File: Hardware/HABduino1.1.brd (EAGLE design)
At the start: 68.5 x 53.4 mm, 43 parts, among them IC2 TPS61201, U1 ARDUINO_SHIELDNO_SILK, U2 LM3480IM3-3.3, U3 TXS0102DCTT

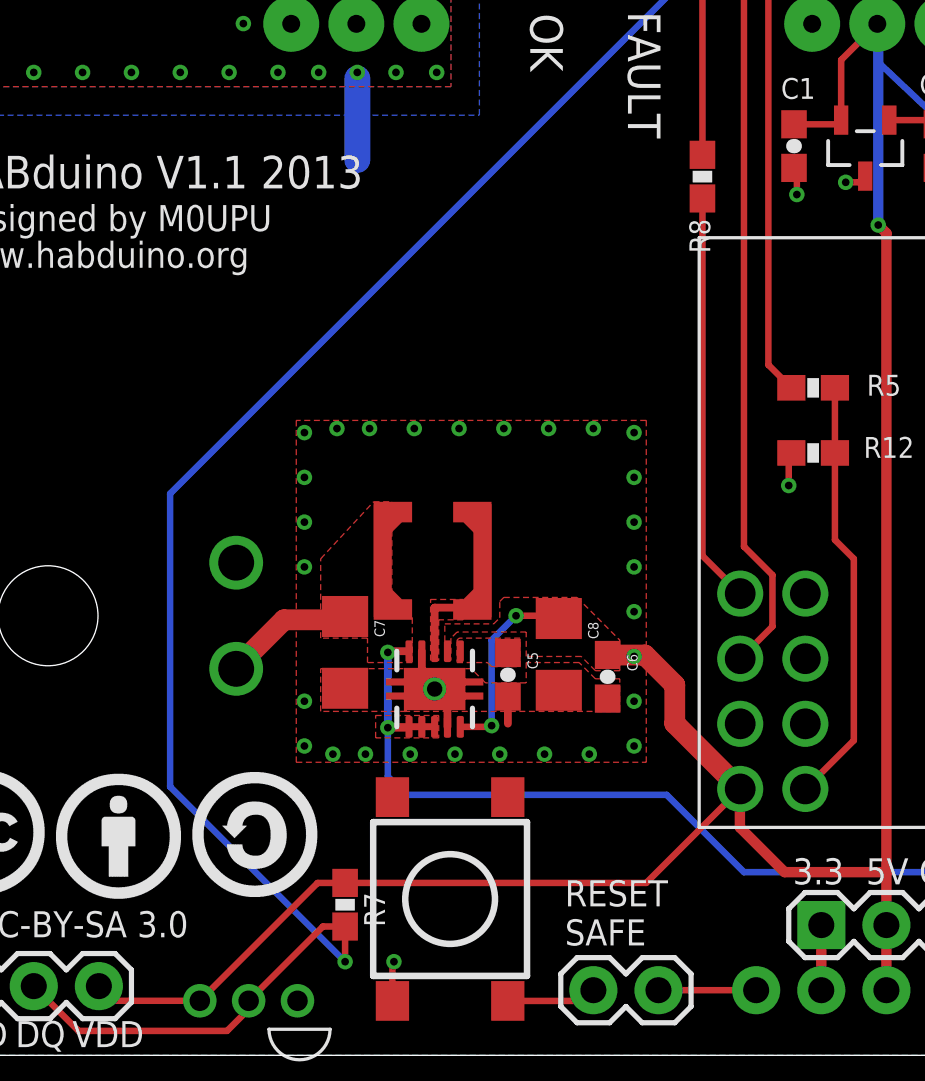
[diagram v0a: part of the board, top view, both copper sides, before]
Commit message: Updated BRD File + Added Sketchup Model
1/ Removed GND via that linked VCC to GND (duh!)
2/ Cleaned up silk screen.
3/ Added location mark to TPS61200 module.
4/ Added Sketchup Model
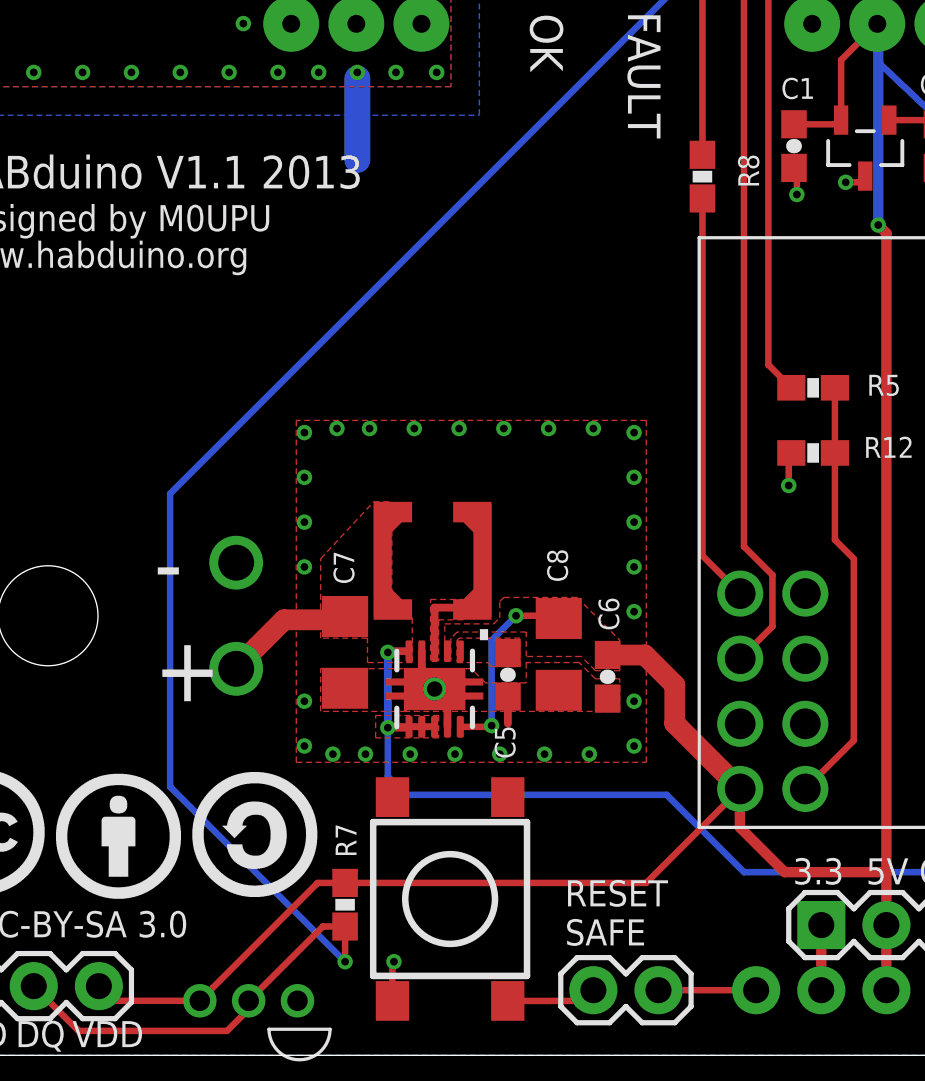
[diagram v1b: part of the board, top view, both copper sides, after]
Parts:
- U$10: value (none) -> 2.2µH
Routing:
- net GND: vias 203 -> 202
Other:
- board text added: "+"
- board text added: "-"
- board text added: "."
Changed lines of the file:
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@@
 <setting verticaltext="up"/>
 </settings>
-<grid distance="0.3175" unitdist="mm" unit="mm" style="lines" multiple="1" display="yes" altdistance="0.025" altunitdist="inch" altunit="inch"/>
+<grid distance="0.15875" unitdist="mm" unit="mm" style="lines" multiple="1" display="yes" altdistance="0.025" altunitdist="inch" altunit="inch"/>
 <layers>
 <layer number="1" name="Top" color="4" fill="1" visible="yes" active="yes"/>
@@
 <layer number="220" name="220bmp" color="21" fill="1" visible="no" active="no"/>
 <layer number="221" name="221bmp" color="22" fill="1" visible="no" active="no"/>
-<layer number="222" name="222bmp" color="23" fill="1" visible="no" active="no"/>
 <layer number="223" name="223bmp" color="24" fill="1" visible="no" active="no"/>
 <layer number="224" name="224bmp" color="25" fill="1" visible="no" active="no"/>
@@
 amateur radio license to
 transmit.</text>
+<text x="9.525" y="13.81125" size="2.54" layer="21" font="vector" ratio="10">+</text>
+<text x="9.525" y="17.93875" size="2.54" layer="21" font="vector" ratio="10">-</text>
+<text x="21.9075" y="16.1925" size="2.54" layer="21" font="vector" ratio="10">.</text>
 </plain>
 <attributes>
@@
 <element name="TEMPINT" library="ava" package="DS1820" value="DS1821" x="15.763875" y="0.85725" rot="R180"/>
 <element name="R7" library="SparkFun" package="0603-RES" value="4K7" x="16.98625" y="5.87375" smashed="yes" rot="R270">
-<attribute name="NAME" x="18.542" y="5.0165" size="0.8128" layer="25" font="vector" ratio="10" rot="R90"/>
+<attribute name="NAME" x="17.43075" y="7.71525" size="0.8128" layer="25" font="vector" ratio="10" rot="R90"/>
 </element>
 <element name="LED1" library="SparkFun" package="LED-0603" value="Green" x="24.812625" y="42.687875" smashed="yes" rot="R180"/>
@@
 <element name="J$2" library="SparkFun" package="SMA-EDGE" value="SMA_EDGE" x="66.3575" y="36.83" rot="R90"/>
 <element name="R8" library="SparkFun" package="0603-RES" value="340K" x="30.9245" y="34.274125" smashed="yes" rot="R270">
-<attribute name="NAME" x="30.4165" y="32.623125" size="0.8128" layer="25" font="vector" ratio="10" rot="R270"/>
+<attribute name="NAME" x="32.3215" y="35.163125" size="0.8128" layer="25" font="vector" ratio="10" rot="R270"/>
 </element>
 <element name="U1" library="SparkFun" package="DUEMILANOVE_VIAS" value="ARDUINO_SHIELDNO_SILK" x="21.59" y="53.34" rot="R270"/>
@@
 <attribute name="OC_FARNELL" value="unknown" x="20.47875" y="14.2875" size="1.778" layer="27" rot="R180" display="off"/>
 </element>
-<element name="C7" library="SparkFun" package="1206" value="10uF" x="16.98625" y="15.71625" rot="R270"/>
-<element name="C8" library="SparkFun" package="1206" value="22uF" x="25.320625" y="15.636875" rot="R270"/>
-<element name="C5" library="SparkFun" package="0603-CAP" value="10µF" x="23.33625" y="14.843125" rot="R270"/>
-<element name="C6" library="SparkFun" package="0603-CAP" value="0.1µF" x="27.225625" y="14.76375" rot="R270"/>
+<element name="C7" library="SparkFun" package="1206" value="10uF" x="16.98625" y="15.71625" smashed="yes" rot="R270">
+<attribute name="NAME" x="16.54175" y="19.685" size="0.8" layer="25" font="vector" ratio="10" rot="R270"/>
+</element>
+<element name="C8" library="SparkFun" package="1206" value="22uF" x="25.320625" y="15.636875" smashed="yes" rot="R270">
+<attribute name="NAME" x="24.876125" y="19.764375" size="0.8" layer="25" font="vector" ratio="10" rot="R270"/>
+</element>
+<element name="C5" library="SparkFun" package="0603-CAP" value="10µF" x="23.33625" y="14.843125" smashed="yes" rot="R270">
+<attribute name="NAME" x="22.82825" y="12.874625" size="0.8" layer="25" font="vector" ratio="10" rot="R270"/>
+</element>
+<element name="C6" library="SparkFun" package="0603-CAP" value="0.1µF" x="27.225625" y="14.76375" smashed="yes" rot="R270">
+<attribute name="NAME" x="26.876375" y="17.87525" size="0.8" layer="25" font="vector" ratio="10" rot="R270"/>
+</element>
 <element name="U$9" library="ava" package="TE_CONNECTIVITY_1-770966-0" value="TE_CONNECTIVITY_1-770966-0" x="5.3975" y="17.145" rot="R270">
 <attribute name="FARNELL" value="1098556" x="5.3975" y="17.145" size="1.778" layer="27" rot="R270" display="off"/>
 </element>
-<element name="U$10" library="StevesCoilCraft" package="COILCRAFT_LPS4018" value="" x="20.399375" y="19.288125"/>
+<element name="U$10" library="StevesCoilCraft" package="COILCRAFT_LPS4018" value="2.2µH" x="20.399375" y="19.288125"/>
 </elements>
 <signals>
@@
 <via x="28.2575" y="19.05" extent="1-16" drill="0.3"/>
 <via x="28.2575" y="17.30375" extent="1-16" drill="0.3"/>
-<via x="28.2575" y="15.5575" extent="1-16" drill="0.3"/>
 <via x="28.2575" y="13.81125" extent="1-16" drill="0.3"/>
 <via x="28.2575" y="24.28875" extent="1-16" drill="0.3"/>
@@
 </signal>
 </signals>
+<errors>
+</errors>
 </board>
 </drawing>
